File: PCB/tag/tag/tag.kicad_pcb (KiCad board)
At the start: 2 copper layers, 22.2 x 19.3 mm, 8 parts, among them J1 SM02B-SRSS-TB LFSN, J2 Conn_ARM_SWD_TagConnect_TC203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, J3 Conn_ARM_JTAG_SWD_10, U1 DWM3001C, U2 TPS79933DDCR

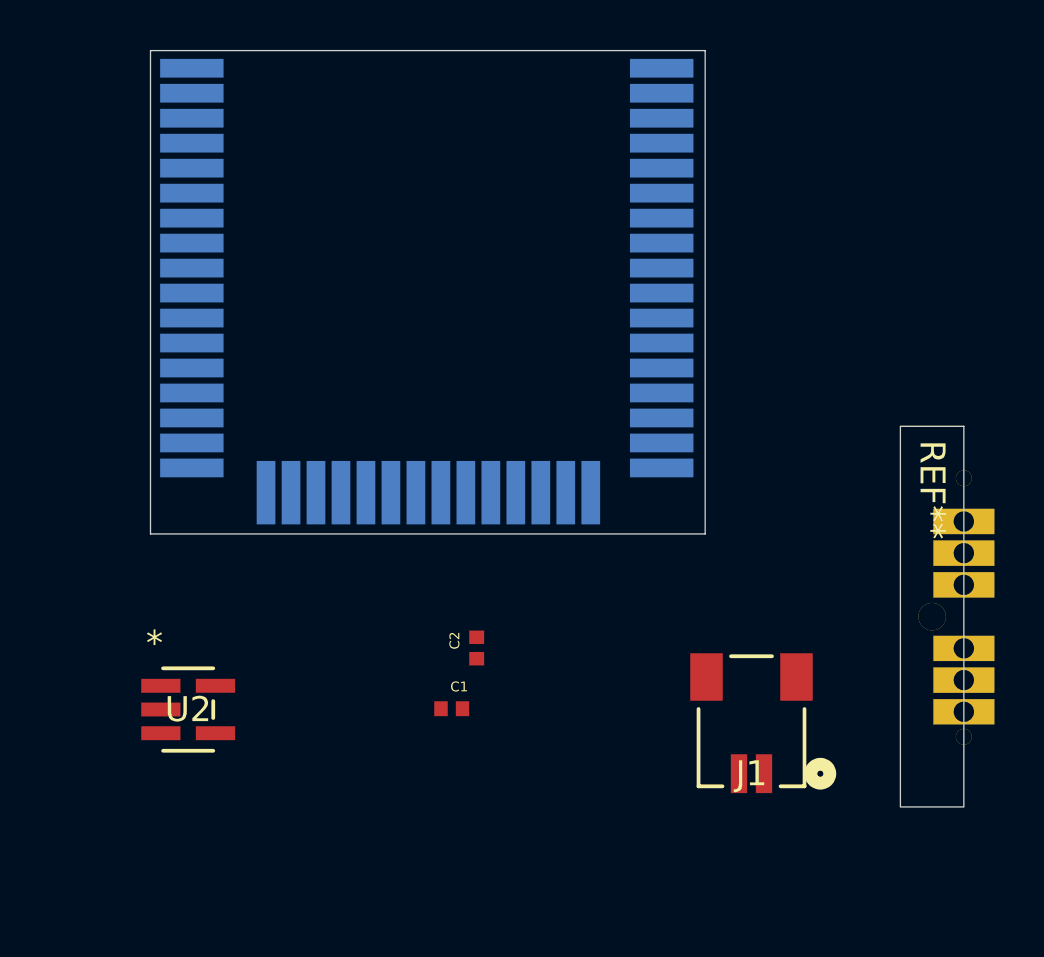
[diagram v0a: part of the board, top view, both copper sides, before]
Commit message: updated anchor pcb + DWM Datasheet
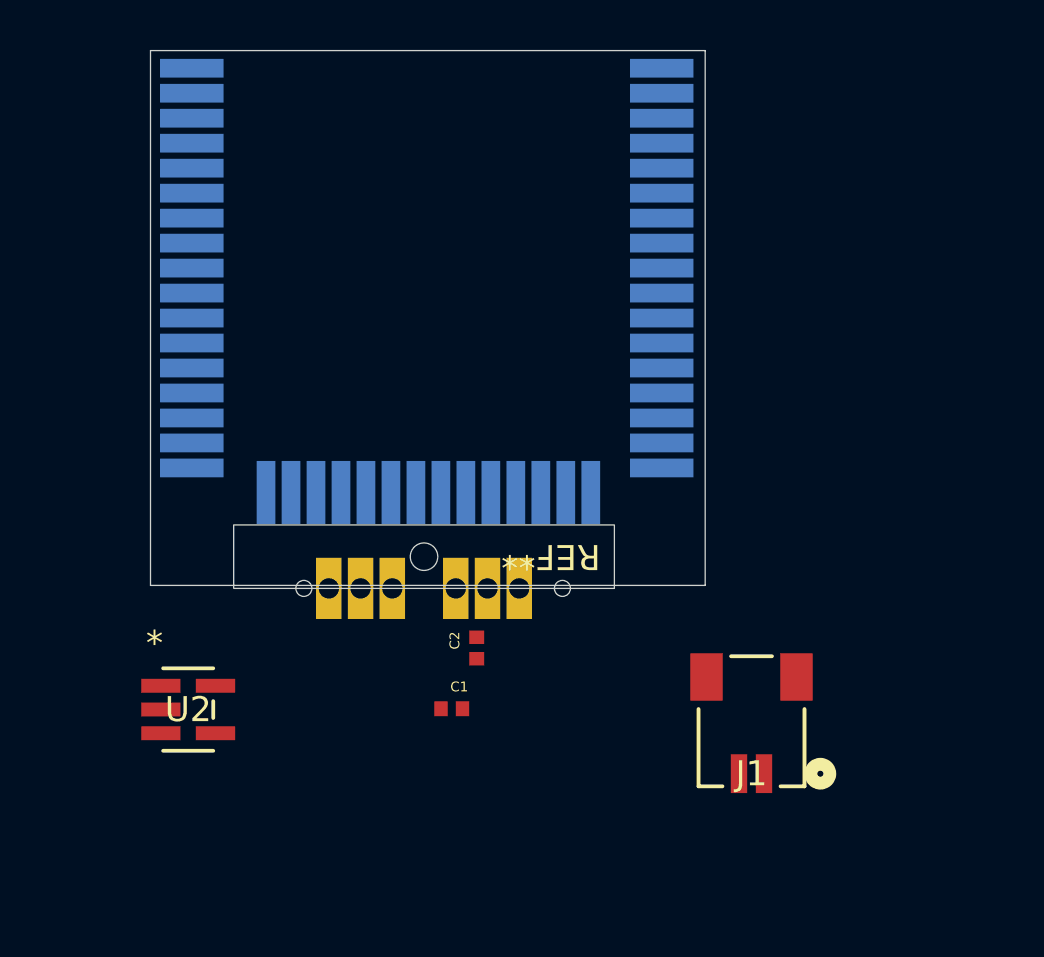
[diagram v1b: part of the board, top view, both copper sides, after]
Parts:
- moved REF** 20.5 mm to (124.9, 89.4), turned to 180 degrees
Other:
- board size 22.2 x 19.3 mm -> 22.2 x 21.4 mm
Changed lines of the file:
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@@
 	(footprint "custom:edgeconnect"
 		(layer "F.Cu")
-		(at 145.23 91.81 -90)
+		(at 124.89 89.41 180)
 		(property "Reference" "REF**"
-			(at -5.08 0 -90)
+			(at -5.08 0 180)
 			(unlocked yes)
 			(layer "F.SilkS")
@@
 		)
 		(property "Value" "edgeconnect"
-			(at -1.5 0 -90)
+			(at -1.5 0 180)
 			(unlocked yes)
 			(layer "F.Fab")
@@
 		)
 		(property "Footprint" "custom:edgeconnect"
-			(at 0 0 -90)
+			(at 0 0 180)
 			(unlocked yes)
 			(layer "F.Fab")
@@
 		)
 		(property "Datasheet" ""
-			(at 0 0 -90)
+			(at 0 0 180)
 			(unlocked yes)
 			(layer "F.Fab")
@@
 		)
 		(property "Description" ""
-			(at 0 0 -90)
+			(at 0 0 180)
 			(unlocked yes)
 			(layer "F.Fab")
@@
 			(end 7.62 1.27)
 			(stroke
-				(width 0.05)
+				(width 0.01)
 				(type default)
 			)
@@
 		)
 		(fp_text user "${REFERENCE}"
-			(at 0.56 0 -90)
+			(at 0.56 0 180)
 			(unlocked yes)
 			(layer "F.Fab")
@@
 			)
 		)
-		(pad "1" thru_hole rect
-			(at 3.81 -1.27 270)
-			(size 1.02 2.45)
-			(drill 0.8128)
-			(property pad_prop_castellated)
-			(layers "*.Cu" "*.Mask")
-			(remove_unused_layers no)
-		)
-		(pad "2" thru_hole rect
-			(at 2.54 -1.27 270)
-			(size 1.02 2.45)
-			(drill 0.8128)
-			(property pad_prop_castellated)
-			(layers "*.Cu" "*.Mask")
-			(remove_unused_layers no)
-		)
-		(pad "3" thru_hole rect
-			(at 1.27 -1.27 270)
-			(size 1.02 2.45)
-			(drill 0.8128)
-			(property pad_prop_castellated)
-			(layers "*.Cu" "*.Mask")
-			(remove_unused_layers no)
-		)
-		(pad "4" thru_hole rect
-			(at -1.27 -1.27 270)
-			(size 1.02 2.45)
-			(drill 0.8128)
-			(property pad_prop_castellated)
-			(layers "*.Cu" "*.Mask")
-			(remove_unused_layers no)
-		)
-		(pad "5" thru_hole rect
-			(at -2.54 -1.27 270)
-			(size 1.02 2.45)
-			(drill 0.8128)
-			(property pad_prop_castellated)
-			(layers "*.Cu" "*.Mask")
-			(remove_unused_layers no)
-		)
-		(pad "6" thru_hole rect
-			(at -3.81 -1.27 270)
-			(size 1.02 2.45)
-			(drill 0.8128)
-			(property pad_prop_castellated)
-			(layers "*.Cu" "*.Mask")
-			(remove_unused_layers no)
-		)
-		(pad "7" thru_hole circle
-			(at 4.81 -1.27 270)
+		(pad "" thru_hole circle
+			(at -5.54 -1.27 180)
 			(size 0.64 0.64)
 			(drill 0.64)
-			(property pad_prop_castellated)
-			(layers "*.Cu" "*.Mask")
+			(layers "*.Mask")
+			(remove_unused_layers no)
+			(zone_connect 0)
+			(teardrops
+				(best_length_ratio 0.2)
+				(max_length 0)
+				(best_width_ratio 0.6)
+				(max_width 0)
+				(curve_points 0)
+				(filter_ratio 0.9)
+				(enabled no)
+				(allow_two_segments no)
+				(prefer_zone_connections no)
+			)
+		)
+		(pad "" thru_hole circle
+			(at 0 0 180)
+			(size 1.1 1.1)
+			(drill 1.1)
+			(layers "*.Mask")
+			(remove_unused_layers no)
+			(zone_connect 0)
+			(teardrops
+				(best_length_ratio 0.2)
+				(max_length 0)
+				(best_width_ratio 0.6)
+				(max_width 0)
+				(curve_points 0)
+				(filter_ratio 0.9)
+				(enabled no)
+				(allow_two_segments yes)
+				(prefer_zone_connections yes)
+			)
+		)
+		(pad "" thru_hole circle
+			(at 4.81 -1.27 180)
+			(size 0.64 0.64)
+			(drill 0.64)
+			(layers "*.Mask")
 			(remove_unused_layers no)
 			(zone_connect 0)
@@
 			)
 		)
-		(pad "8" thru_hole circle
-			(at -5.54 -1.27 270)
-			(size 0.64 0.64)
-			(drill 0.64)
+		(pad "1" thru_hole rect
+			(at 3.81 -1.27 180)
+			(size 1.02 2.45)
+			(drill 0.8128)
 			(property pad_prop_castellated)
 			(layers "*.Cu" "*.Mask")
 			(remove_unused_layers no)
-			(zone_connect 0)
-			(teardrops
-				(best_length_ratio 0.2)
-				(max_length 0)
-				(best_width_ratio 0.6)
-				(max_width 0)
-				(curve_points 0)
-				(filter_ratio 0.9)
-				(enabled no)
-				(allow_two_segments no)
-				(prefer_zone_connections no)
-			)
-		)
-		(pad "9" thru_hole circle
-			(at 0 0 270)
-			(size 1.1 1.1)
-			(drill 1.1)
+		)
+		(pad "2" thru_hole rect
+			(at 2.54 -1.27 180)
+			(size 1.02 2.45)
+			(drill 0.8128)
 			(property pad_prop_castellated)
 			(layers "*.Cu" "*.Mask")
 			(remove_unused_layers no)
-			(zone_connect 0)
-			(teardrops
-				(best_length_ratio 0.2)
-				(max_length 0)
-				(best_width_ratio 0.6)
-				(max_width 0)
-				(curve_points 0)
-				(filter_ratio 0.9)
-				(enabled no)
-				(allow_two_segments yes)
-				(prefer_zone_connections yes)
-			)
+		)
+		(pad "3" thru_hole rect
+			(at 1.27 -1.27 180)
+			(size 1.02 2.45)
+			(drill 0.8128)
+			(property pad_prop_castellated)
+			(layers "*.Cu" "*.Mask")
+			(remove_unused_layers no)
+		)
+		(pad "4" thru_hole rect
+			(at -1.27 -1.27 180)
+			(size 1.02 2.45)
+			(drill 0.8128)
+			(property pad_prop_castellated)
+			(layers "*.Cu" "*.Mask")
+			(remove_unused_layers no)
+		)
+		(pad "5" thru_hole rect
+			(at -2.54 -1.27 180)
+			(size 1.02 2.45)
+			(drill 0.8128)
+			(property pad_prop_castellated)
+			(layers "*.Cu" "*.Mask")
+			(remove_unused_layers no)
+		)
+		(pad "6" thru_hole rect
+			(at -3.81 -1.27 180)
+			(size 1.02 2.45)
+			(drill 0.8128)
+			(property pad_prop_castellated)
+			(layers "*.Cu" "*.Mask")
+			(remove_unused_layers no)
 		)
 	)
@@
 	(gr_rect
 		(start 113.94 69.15)
-		(end 136.145 88.5)
+		(end 136.145 90.56)
 		(stroke
 			(width 0.05)

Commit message: final tag
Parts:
- removed J2: Conn_ARM_SWD_TagConnect_TC2030-NL, Connector:Tag-Connect_TC2030-IDC-NL_2x03_P1.27mm_Vertical
- removed the REF** at (124.9, 89.4)
- added C3: 100nF, Capacitor_SMD:C_0603_1608Metric, F.Cu at (75.0, 38.8)
- added C4: 10uF, imported:GRM155C80J225KE95D, F.Cu at (72.1, 37.8)
- added D1: APHBM2012LSURKSYKC, imported:LED_APHBM2012LSURKSYKC, F.Cu at (69.5, 38.4)
- added D2: 150060RS75000, imported:WL-SMCW_0603, F.Cu at (65.0, 39.3)
- added D3: 150060RS75000, imported:WL-SMCW_0603, F.Cu at (59.1, 39.0)
- added J4: TSM-102-01-X-SV, imported:SAMTEC_TSM-102-01-X-SV, F.Cu at (79.2, 39.9)
- added J5: TSM-102-01-X-SV, imported:SAMTEC_TSM-102-01-X-SV, F.Cu at (60.1, 30.1)
- added J6: TSM-102-01-X-SV, imported:SAMTEC_TSM-102-01-X-SV, F.Cu at (66.2, 43.7)
- added J7: TSM-102-01-X-SV, imported:SAMTEC_TSM-102-01-X-SV, F.Cu at (60.3, 43.8)
- added Q1: IRLML2402TRPBF, digikey-footprints:SOT-23-3, F.Cu at (65.7, 28.7)
- added Q2: IRLML2402TRPBF, digikey-footprints:SOT-23-3, F.Cu at (59.3, 36.0)
- added R1: 1K5, Resistor_SMD:R_0402_1005Metric, F.Cu at (68.7, 27.1)
- added R2: 1K5, Resistor_SMD:R_0402_1005Metric, F.Cu at (62.1, 34.0)
- added R3: 100K, Resistor_SMD:R_0402_1005Metric, F.Cu at (70.4, 32.5)
- added R4: 100K, Resistor_SMD:R_0402_1005Metric, F.Cu at (62.4, 35.8)
- added R5: 150, Resistor_SMD:R_0402_1005Metric, F.Cu at (66.7, 36.7)
- added R6: 820, Resistor_SMD:R_0402_1005Metric, F.Cu at (69.9, 34.9)
- added R7: 1k8, Resistor_SMD:R_0402_1005Metric, F.Cu at (67.2, 39.2)
- added R8: 1k8, Resistor_SMD:R_0402_1005Metric, F.Cu at (62.6, 39.1)
- added REF**: Edge-Connect-THT, imported:Edge-Connect-THT, F.Cu at (83.8, 33.9)
- added S1: TL3315NF160Q, digikey-footprints:Switch_Tactile_SMD_4.5x4.5mm_TL3315NF160Q, F.Cu at (66.4, 33.4)
- added TP1: Vgnd, TestPoint:TestPoint_Pad_D1.0mm, F.Cu at (75.2, 36.0)
- added TP2: Vbatt, TestPoint:TestPoint_Pad_D1.0mm, F.Cu at (72.4, 39.8)
- added TP3: Vreg, TestPoint:TestPoint_Pad_D1.0mm, F.Cu at (68.7, 29.3)
- moved J1 84.1 mm to (72.0, 43.9)
- moved U1 69.0 mm to (80.4, 44.2)
- moved C1 67.3 mm to (81.3, 45.1), turned to 90 degrees
- moved C2 66.9 mm to (79.9, 45.5)
- moved U2 63.2 mm to (77.0, 45.4)
- moved J3 53.2 mm to (75.3, 30.2), turned to 180 degrees
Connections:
- net Net-(J2-SWCLK) renamed /SWD_CLK
- net Net-(J2-SWDIO) renamed /SWD_DIO
- net Net-(U2-EN) renamed Vbatt +3.7V
- net RESET renamed /RST
- C1 pad 2: Vreg -> Vreg +3.3V
- J3 pad 1: Vreg -> Vreg +3.3V
- U1 pad 12: Vreg -> /3001vdd
- U1 pad 44: unconnected-(U1-DW_GP3-Pad44) -> Net-(U1-DW_GP3)
- U1 pad 45: unconnected-(U1-DW_GP2-Pad45) -> Net-(U1-DW_GP2)
- U1 pad 6: unconnected-(U1-P0.17-Pad6) -> Net-(U1-P0.17)
- U1 pad 7: unconnected-(U1-P0.14-Pad7) -> Net-(U1-P0.14)
- U2 pad 5: Vreg -> Vreg +3.3V
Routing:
- net GND: track 0.00 -> 138.5 mm, vias 0 -> 9
- net Vreg +3.3V: track 0.00 -> 58.2 mm, vias 0 -> 3
- net /RST: track 0.00 -> 44.6 mm, vias 0 -> 3
- net Net-(Q1-S): track 0.00 -> 43.6 mm, vias 0 -> 4
- net /SWD_DIO: track 0.00 -> 28.7 mm, vias 0 -> 3
- net Net-(U1-P0.17): track 0.00 -> 26.4 mm, vias 0 -> 3
- net Net-(D1-K1): track 0.00 -> 25.6 mm, vias 0 -> 2
- net /3001vdd: track 0.00 -> 24.3 mm, vias 0 -> 2
- net Net-(U1-P0.14): track 0.00 -> 21.8 mm, vias 0 -> 1
- net /SWD_CLK: track 0.00 -> 21.3 mm, vias 0 -> 1
- net Net-(U1-DW_GP3): track 0.00 -> 16.0 mm, vias 0 -> 3
- net Vbatt +3.7V: track 0.00 -> 15.1 mm
- net Net-(D1-K2): track 0.00 -> 12.5 mm, vias 0 -> 2
- net Net-(Q1-G): track 0.00 -> 10.7 mm, vias 0 -> 2
- net Net-(U1-DW_GP2): track 0.00 -> 7.61 mm, vias 0 -> 1
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- added copper zone on B.Cu, net GND
- added copper zone on F.Cu, net GND
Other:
- board size 22.2 x 21.4 mm -> 26.8 x 21.3 mm
- rule pad_to_mask_clearance: 0 -> 0.0508
